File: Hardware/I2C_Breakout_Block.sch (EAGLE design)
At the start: 23 parts, among them U2 PCA9306

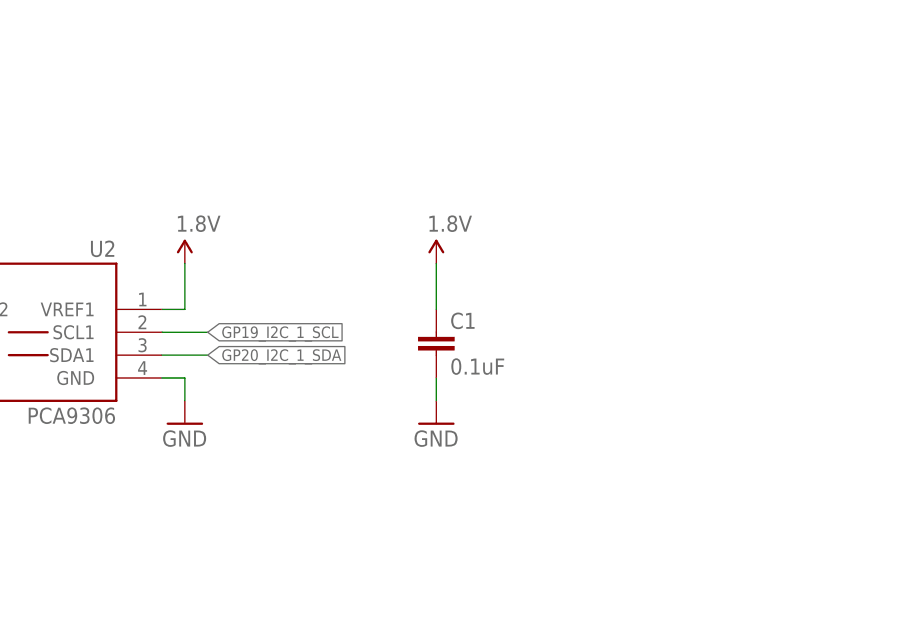
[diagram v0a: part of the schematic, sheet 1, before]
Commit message: repalced I2C resistors
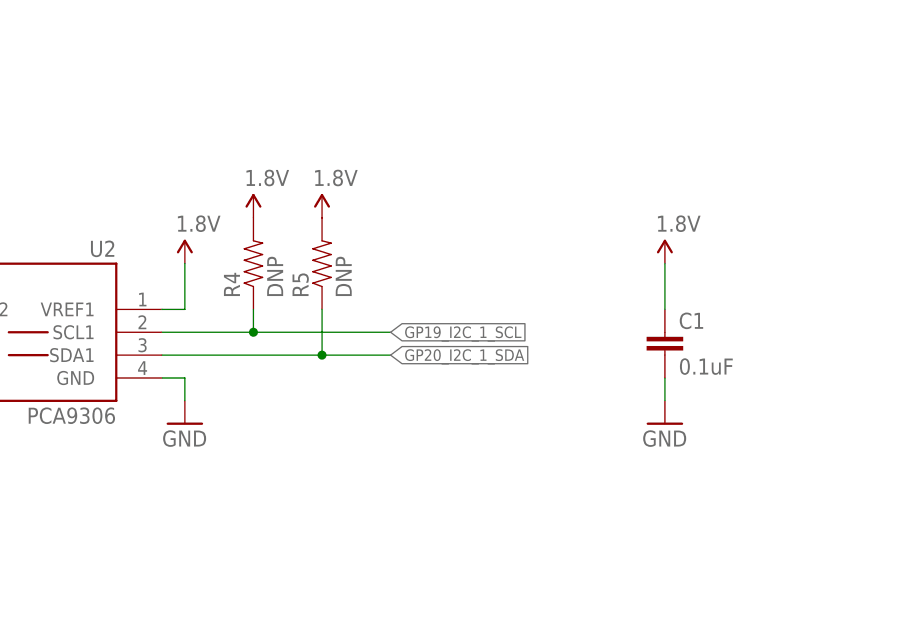
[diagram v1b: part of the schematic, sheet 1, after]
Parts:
- added R4, R5: DNP, SparkFun-Resistors:2.2KOHM1/10W1%(0603)
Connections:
- net 1.8V: now also R4.2, R5.2
- net GP19_I2C_1_SCL: now also R4.1
- net GP20_I2C_1_SDA: now also R5.1
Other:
- moved on the sheet: C1
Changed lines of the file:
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@@
 <part name="GND8" library="SparkFun-Aesthetics" deviceset="GND" device=""/>
 <part name="GND9" library="SparkFun-Aesthetics" deviceset="GND" device=""/>
+<part name="R4" library="SparkFun-Resistors" deviceset="2.2KOHM1/10W1%(0603)" device="" value="DNP"/>
+<part name="R5" library="SparkFun-Resistors" deviceset="2.2KOHM1/10W1%(0603)" device="" value="DNP"/>
+<part name="SUPPLY2" library="SparkFun-Aesthetics" deviceset="1.8V" device=""/>
+<part name="SUPPLY3" library="SparkFun-Aesthetics" deviceset="1.8V" device=""/>
 </parts>
 <sheets>
@@
 <instance part="FID4" gate="G$1" x="246.38" y="30.48"/>
 <instance part="GND1" gate="1" x="96.52" y="63.5"/>
-<instance part="C1" gate="G$1" x="190.5" y="76.2"/>
+<instance part="C1" gate="G$1" x="215.9" y="76.2"/>
 <instance part="C2" gate="G$1" x="66.04" y="76.2"/>
 <instance part="GND2" gate="1" x="66.04" y="68.58"/>
-<instance part="GND6" gate="1" x="190.5" y="68.58"/>
-<instance part="SUPPLY1" gate="G$1" x="190.5" y="86.36"/>
+<instance part="GND6" gate="1" x="215.9" y="68.58"/>
+<instance part="SUPPLY1" gate="G$1" x="215.9" y="86.36"/>
 <instance part="JP2" gate="G$1" x="86.36" y="76.2" rot="MR180"/>
 <instance part="SJ1" gate="G$1" x="101.6" y="101.6" rot="R180"/>
@@
 <instance part="GND8" gate="1" x="142.24" y="121.92"/>
 <instance part="GND9" gate="1" x="114.3" y="121.92"/>
+<instance part="R4" gate="G$1" x="170.18" y="86.36" rot="R90"/>
+<instance part="R5" gate="G$1" x="177.8" y="86.36" rot="R90"/>
+<instance part="SUPPLY2" gate="G$1" x="170.18" y="91.44"/>
+<instance part="SUPPLY3" gate="G$1" x="177.8" y="91.44"/>
 </instances>
 <busses>
@@
 <pinref part="C1" gate="G$1" pin="2"/>
 <pinref part="GND6" gate="1" pin="GND"/>
-<wire x1="190.5" y1="71.12" x2="190.5" y2="73.66" width="0.1524" layer="91"/>
+<wire x1="215.9" y1="71.12" x2="215.9" y2="73.66" width="0.1524" layer="91"/>
 </segment>
 <segment>
@@
 <pinref part="C1" gate="G$1" pin="1"/>
 <pinref part="SUPPLY1" gate="G$1" pin="1.8V"/>
-<wire x1="190.5" y1="86.36" x2="190.5" y2="81.28" width="0.1524" layer="91"/>
+<wire x1="215.9" y1="86.36" x2="215.9" y2="81.28" width="0.1524" layer="91"/>
+</segment>
+<segment>
+<pinref part="R4" gate="G$1" pin="2"/>
+<pinref part="SUPPLY2" gate="G$1" pin="1.8V"/>
+</segment>
+<segment>
+<pinref part="R5" gate="G$1" pin="2"/>
+<pinref part="SUPPLY3" gate="G$1" pin="1.8V"/>
 </segment>
 </net>
@@
 <segment>
 <pinref part="U2" gate="G$1" pin="SCL1"/>
-<wire x1="160.02" y1="78.74" x2="165.1" y2="78.74" width="0.1524" layer="91"/>
-<label x="165.1" y="78.74" size="1.27" layer="95" xref="yes"/>
+<wire x1="160.02" y1="78.74" x2="170.18" y2="78.74" width="0.1524" layer="91"/>
+<label x="185.42" y="78.74" size="1.27" layer="95" xref="yes"/>
+<pinref part="R4" gate="G$1" pin="1"/>
+<wire x1="170.18" y1="78.74" x2="185.42" y2="78.74" width="0.1524" layer="91"/>
+<wire x1="170.18" y1="81.28" x2="170.18" y2="78.74" width="0.1524" layer="91"/>
+<junction x="170.18" y="78.74"/>
 </segment>
 </net>
@@
 <segment>
 <pinref part="U2" gate="G$1" pin="SDA1"/>
-<wire x1="160.02" y1="76.2" x2="165.1" y2="76.2" width="0.1524" layer="91"/>
-<label x="165.1" y="76.2" size="1.27" layer="95" xref="yes"/>
+<wire x1="160.02" y1="76.2" x2="177.8" y2="76.2" width="0.1524" layer="91"/>
+<label x="185.42" y="76.2" size="1.27" layer="95" xref="yes"/>
+<pinref part="R5" gate="G$1" pin="1"/>
+<wire x1="177.8" y1="76.2" x2="185.42" y2="76.2" width="0.1524" layer="91"/>
+<wire x1="177.8" y1="81.28" x2="177.8" y2="76.2" width="0.1524" layer="91"/>
+<junction x="177.8" y="76.2"/>
 </segment>
 </net>

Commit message: Rev to 10, fix gnd/pwr/text
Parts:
- R1, R2: value 2.2k -> 10K; device SparkFun-Resistors:2.2KOHM1/10W1%(0603) -> SparkFun-Resistors:10KOHM1/10W1%(0603)0603
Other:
- note added: "v10"
- note removed: "v02"
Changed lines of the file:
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@@
 <?xml version="1.0" encoding="utf-8"?>
 <!DOCTYPE eagle SYSTEM "eagle.dtd">
-<eagle version="6.5.0">
+<eagle version="6.6.0">
 <drawing>
 <settings>
@@
 <layer number="254" name="cooling" color="7" fill="1" visible="yes" active="yes"/>
 </layers>
-<schematic xreflabel="%F%N/%S" xrefpart="1_/%S.%C%R">
+<schematic xreflabel="%F%N/%S" xrefpart="/%S.%C%R">
 <attributes>
 </attributes>
@@
 <part name="GND4" library="supply1" deviceset="GND" device=""/>
 <part name="FRAME2" library="SparkFun-Aesthetics" deviceset="FRAME-LETTER" device=""/>
-<part name="R1" library="SparkFun-Resistors" deviceset="2.2KOHM1/10W1%(0603)" device="" value="2.2k"/>
-<part name="R2" library="SparkFun-Resistors" deviceset="2.2KOHM1/10W1%(0603)" device="" value="2.2k"/>
+<part name="R1" library="SparkFun-Resistors" deviceset="10KOHM1/10W1%(0603)" device="0603" value="10K"/>
+<part name="R2" library="SparkFun-Resistors" deviceset="10KOHM1/10W1%(0603)" device="0603" value="10K"/>
 <part name="U2" library="SparkFun-DigitalIC" deviceset="PCA9306" device="PCA9306DC-1:1" value="PCA9306"/>
 <part name="SUPPLY4" library="SparkFun-Aesthetics" deviceset="1.8V" device=""/>
@@
 <plain>
 <text x="167.64" y="10.16" size="2.54" layer="94" ratio="15">Casey Kuhns</text>
-<text x="238.76" y="7.62" size="2.54" layer="94" ratio="15">v02</text>
+<text x="238.76" y="7.62" size="2.54" layer="94" ratio="15">v10</text>
 <text x="104.14" y="106.68" size="1.27" layer="97">Note: Default VOUT is 3.3v regulated.</text>
 </plain>
